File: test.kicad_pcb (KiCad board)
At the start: 2 copper layers, 78.7 x 41.3 mm, 36 parts, among them J1 Serial header, J2 AVR-ISP-6, J3 5v Power, J4 INT0/1, J5 Servo, J6 Servo power, J7 I2C Header, Q1 2N7000, SW1 INT0, SW2 INT1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

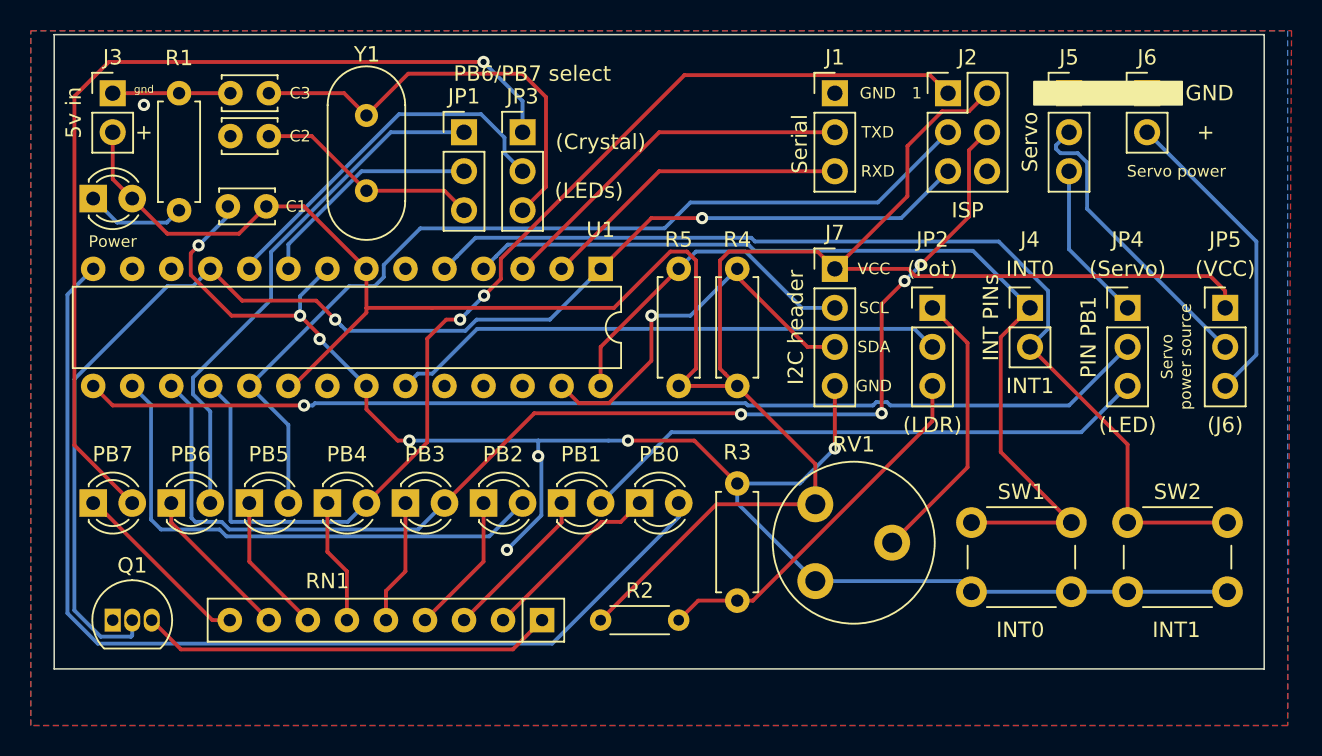
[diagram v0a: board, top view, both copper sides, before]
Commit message: Schema error in PD5 fixed, sent to JLCPCB
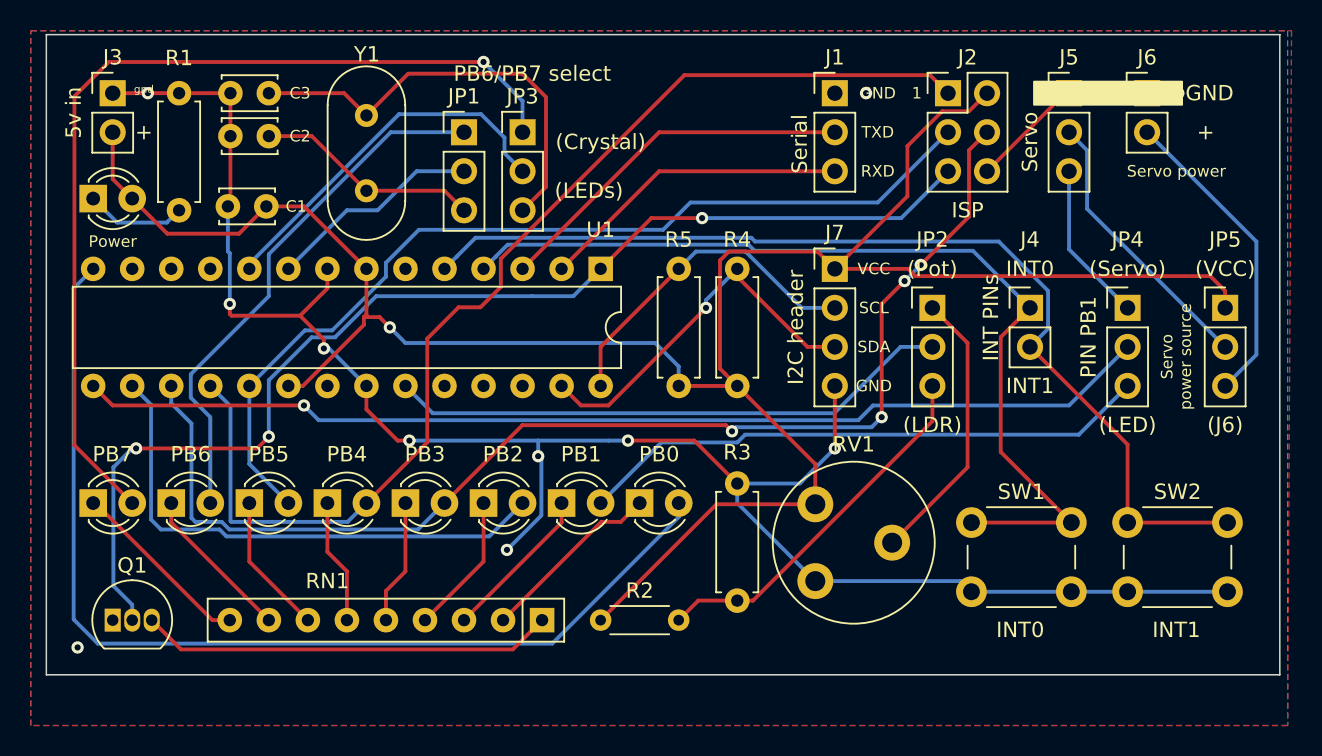
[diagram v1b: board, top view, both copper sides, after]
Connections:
- U1 pad 11: Net-(J2-Pad5) -> Net-(U1-Pad11)
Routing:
- net GND: track 114.2 -> 133.2 mm, vias 9 -> 11
- net Net-(J2-Pad5): track 86.3 -> 74.8 mm, vias 2 -> 3
- net VCC: track 156.4 -> 148.0 mm, vias 0 -> 1
- net Net-(J5-Pad2): track 19.5 -> 18.2 mm
- net Net-(J7-Pad3): track 26.0 -> 24.7 mm
- net Net-(JP1-Pad2): track 15.0 -> 14.1 mm
- net Net-(D6-Pad2): track 73.3 -> 73.6 mm, vias 2 -> 0
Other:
- board size 78.7 x 41.3 mm -> 80.3 x 41.7 mm
